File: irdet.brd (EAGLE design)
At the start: 50 x 45 mm, 66 parts, among them IC1 MEGA8-AI, IC2 78L05F, J1 PSH02-04WG, J2 PSH02-04WG, J3 PSH02-04WG, J4 PSH02-04WG, J5 22-05-7098-09, T1 BC847, T2 BC857, T3 BC847, T4 BC857, T5 BC847, T6 BC857, T7 BC847, T8 BC857, X1 MVE252-5-V, X2 MVE252-5-V

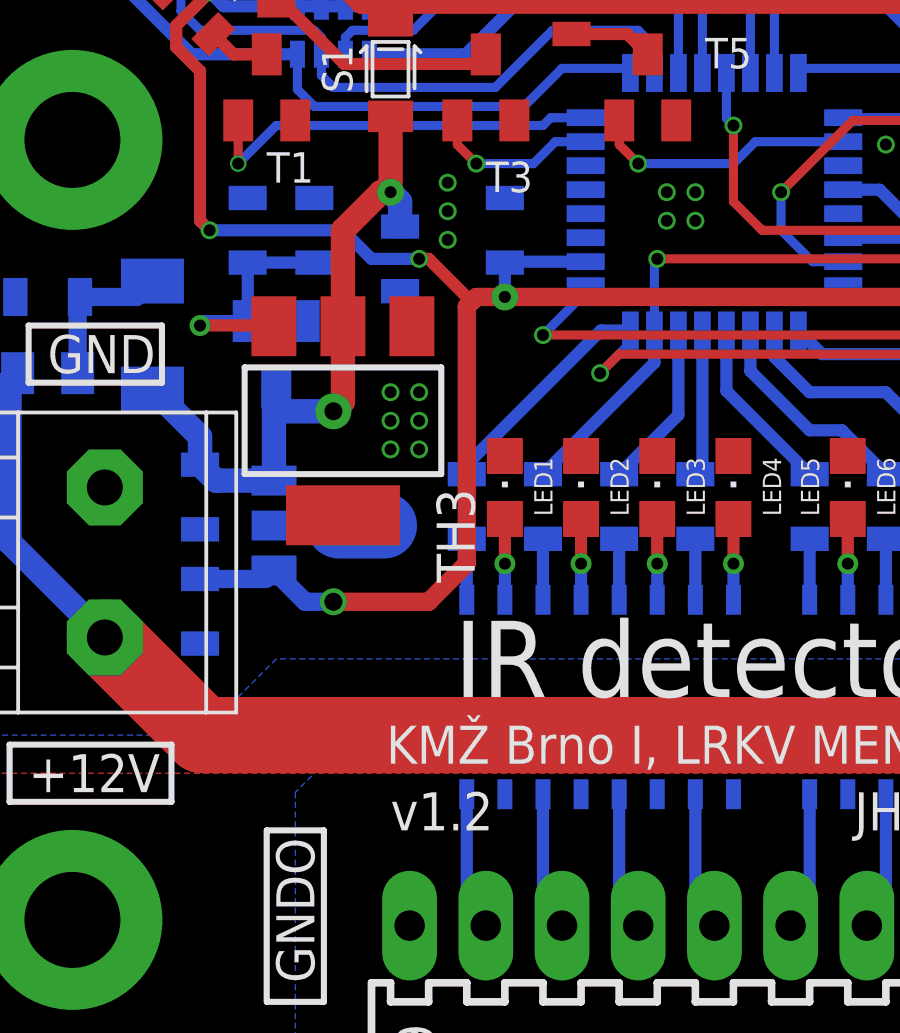
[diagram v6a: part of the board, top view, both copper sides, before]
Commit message: Fix shortcut on PCB.
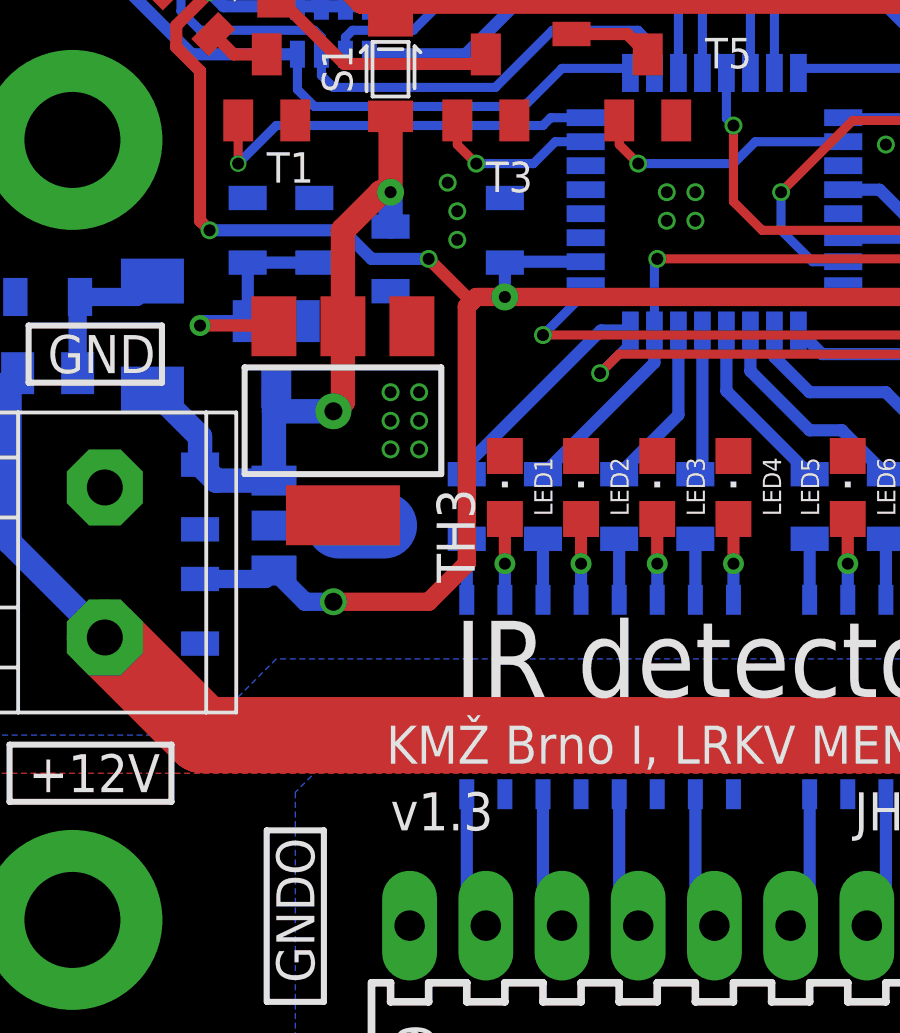
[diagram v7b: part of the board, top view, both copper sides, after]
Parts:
- moved C16 0.32 mm to (14.6, 26.0)
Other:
- board text added: "v1.3"
- board text removed: "v1.2"
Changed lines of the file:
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@@
 <text x="25.4" y="9.2075" size="1.27" layer="25" align="bottom-center">KMŽ Brno I, LRKV MENDELU</text>
 <text x="36.195" y="6.985" size="1.27" layer="25" align="bottom-right">JH 2021</text>
-<text x="14.605" y="6.985" size="1.27" layer="25">v1.2</text>
+<text x="14.605" y="6.985" size="1.27" layer="25">v1.3</text>
 <text x="42.545" y="27.94" size="1.27" layer="25" rot="R90">⏚</text>
 <text x="37.465" y="27.94" size="0.8128" layer="25" rot="R90">VCC</text>
@@
 <attribute name="VALUE" x="46.0375" y="35.56" size="1.016" layer="28" rot="MR90"/>
 </element>
-<element name="C16" library="rcl" package="C0805" value="22u" x="14.9225" y="26.035" smashed="yes" rot="MR270">
-<attribute name="LCSC_PART" value="C45783" x="14.9225" y="26.035" size="1.778" layer="28" rot="MR270" display="off"/>
-<attribute name="NAME" x="14.605" y="24.13" size="1.016" layer="26" rot="MR180"/>
-<attribute name="VALUE" x="13.97" y="27.305" size="1.016" layer="28" rot="MR270"/>
+<element name="C16" library="rcl" package="C0805" value="22u" x="14.605" y="26.035" smashed="yes" rot="MR270">
+<attribute name="LCSC_PART" value="C45783" x="14.605" y="26.035" size="1.778" layer="28" rot="MR270" display="off"/>
+<attribute name="NAME" x="14.2875" y="24.13" size="1.016" layer="26" rot="MR180"/>
+<attribute name="VALUE" x="13.6525" y="27.305" size="1.016" layer="28" rot="MR270"/>
 </element>
 <element name="C2" library="rcl" package="C0805" value="100n" x="32.385" y="27.94" smashed="yes" rot="MR270">
@@
 </polygon>
 <via x="16.51" y="28.575" extent="1-16" drill="0.4" diameter="0.6"/>
-<via x="16.51" y="27.6225" extent="1-16" drill="0.4" diameter="0.6"/>
-<via x="16.51" y="26.67" extent="1-16" drill="0.4" diameter="0.6"/>
+<via x="16.8275" y="27.6225" extent="1-16" drill="0.4" diameter="0.6"/>
+<via x="16.8275" y="26.67" extent="1-16" drill="0.4" diameter="0.6"/>
 <via x="14.605" y="19.685" extent="1-16" drill="0.4" diameter="0.6"/>
 <via x="15.5575" y="19.685" extent="1-16" drill="0.4" diameter="0.6"/>
@@
 <via x="8.5725" y="26.9875" extent="1-16" drill="0.4" diameter="0.6"/>
 <wire x1="13.0175" y1="26.9875" x2="13.97" y2="26.035" width="0.4064" layer="16"/>
-<wire x1="13.97" y1="26.035" x2="15.5575" y2="26.035" width="0.4064" layer="16"/>
-<via x="15.5575" y="26.035" extent="1-16" drill="0.4" diameter="0.6"/>
+<wire x1="13.97" y1="26.035" x2="15.875" y2="26.035" width="0.4064" layer="16"/>
+<via x="15.875" y="26.035" extent="1-16" drill="0.4" diameter="0.6"/>
 <wire x1="8.5725" y1="26.9875" x2="13.0175" y2="26.9875" width="0.4064" layer="16"/>
 <wire x1="17.145" y1="24.4475" x2="17.30375" y2="24.60625" width="0.6096" layer="1"/>
 <wire x1="17.30375" y1="24.60625" x2="17.4625" y2="24.765" width="0.6096" layer="1"/>
 <wire x1="17.4625" y1="24.765" x2="18.415" y2="24.765" width="0.6096" layer="1"/>
-<wire x1="15.5575" y1="26.035" x2="15.875" y2="26.035" width="0.4064" layer="1"/>
 <wire x1="15.875" y1="26.035" x2="17.30375" y2="24.60625" width="0.4064" layer="1"/>
 </signal>
@@
 <wire x1="14.605" y1="28.2575" x2="14.2875" y2="28.2575" width="0.8128" layer="1"/>
 <wire x1="14.2875" y1="28.2575" x2="13.0175" y2="26.9875" width="0.8128" layer="1"/>
-<wire x1="14.9225" y1="27.112" x2="14.9225" y2="27.94" width="0.8128" layer="16"/>
-<wire x1="14.9225" y1="27.94" x2="14.605" y2="28.2575" width="0.8128" layer="16"/>
+<wire x1="14.605" y1="27.112" x2="14.605" y2="28.2575" width="0.8128" layer="16"/>
 <via x="14.605" y="28.2575" extent="1-16" drill="0.4" diameter="0.9"/>
 </signal>
